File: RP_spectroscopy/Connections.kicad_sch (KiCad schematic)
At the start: 32 parts, among them J1 Extension connector 1, J2 Extension connector 2, J3 Conn_Coaxial, J4 Conn_Coaxial, J5 Conn_Coaxial, J6 Conn_Coaxial, J7 Conn_01x04_MountingPin, J8 Conn_01x04_MountingPin, U4 MC78L05_SOT89, U5 L79L05_SOT89

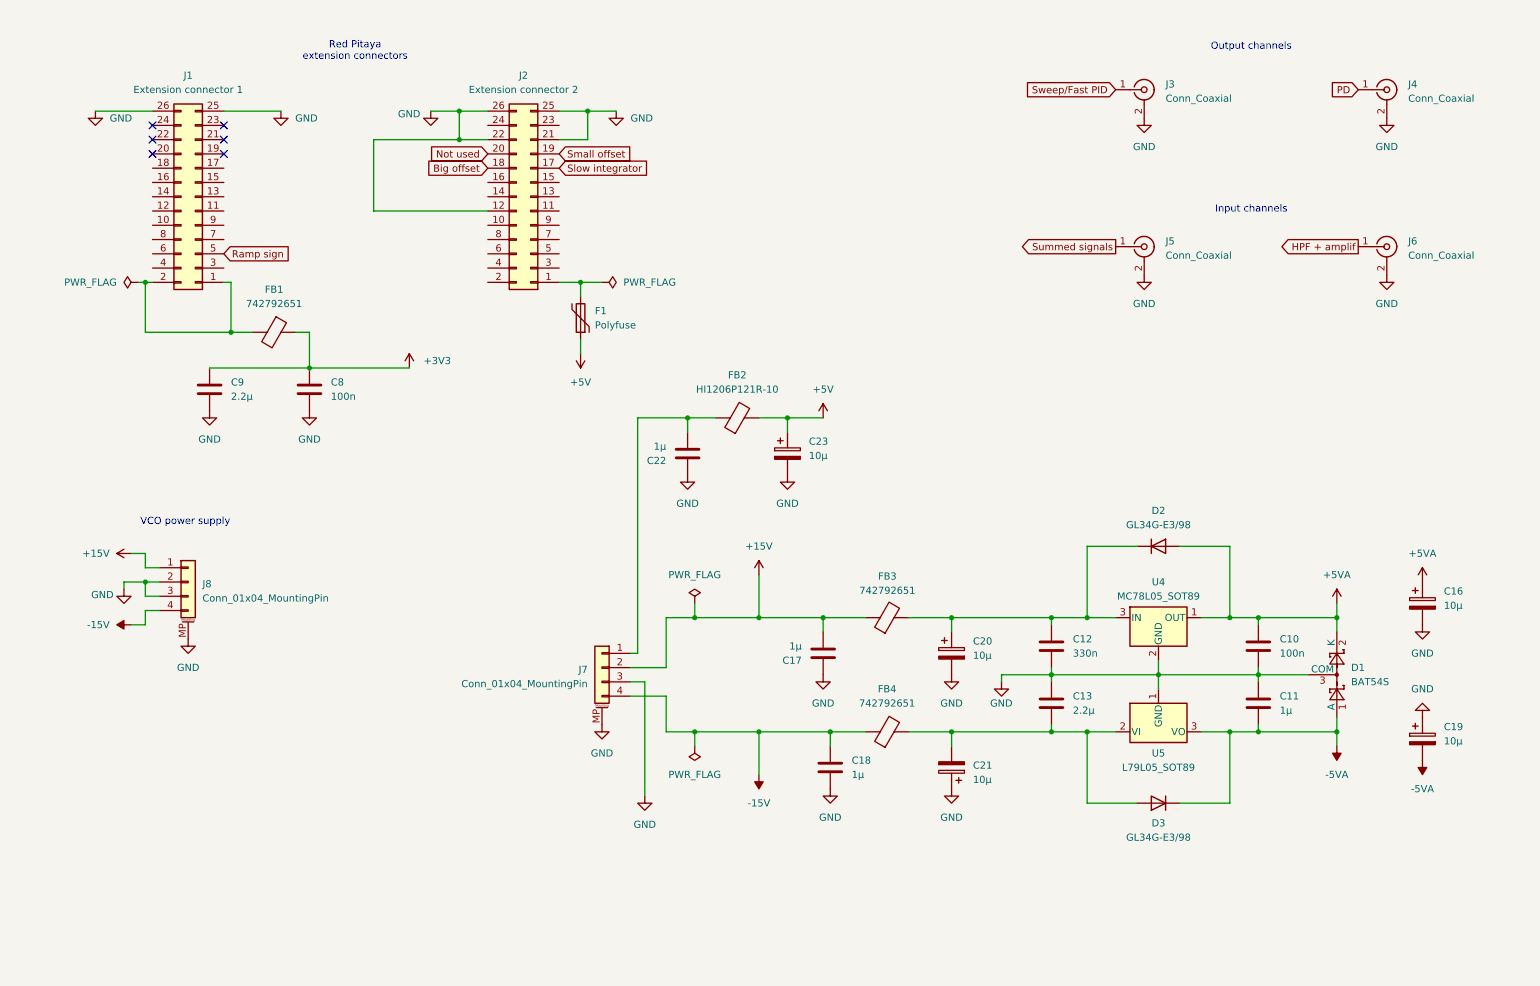
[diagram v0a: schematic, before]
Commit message: Check of the availability of all the components and of the footprints. Added the demultiplexer part of the circuit. Some graphical changes. Changed the values of some R in order to match the ones available in the officina elettronica.
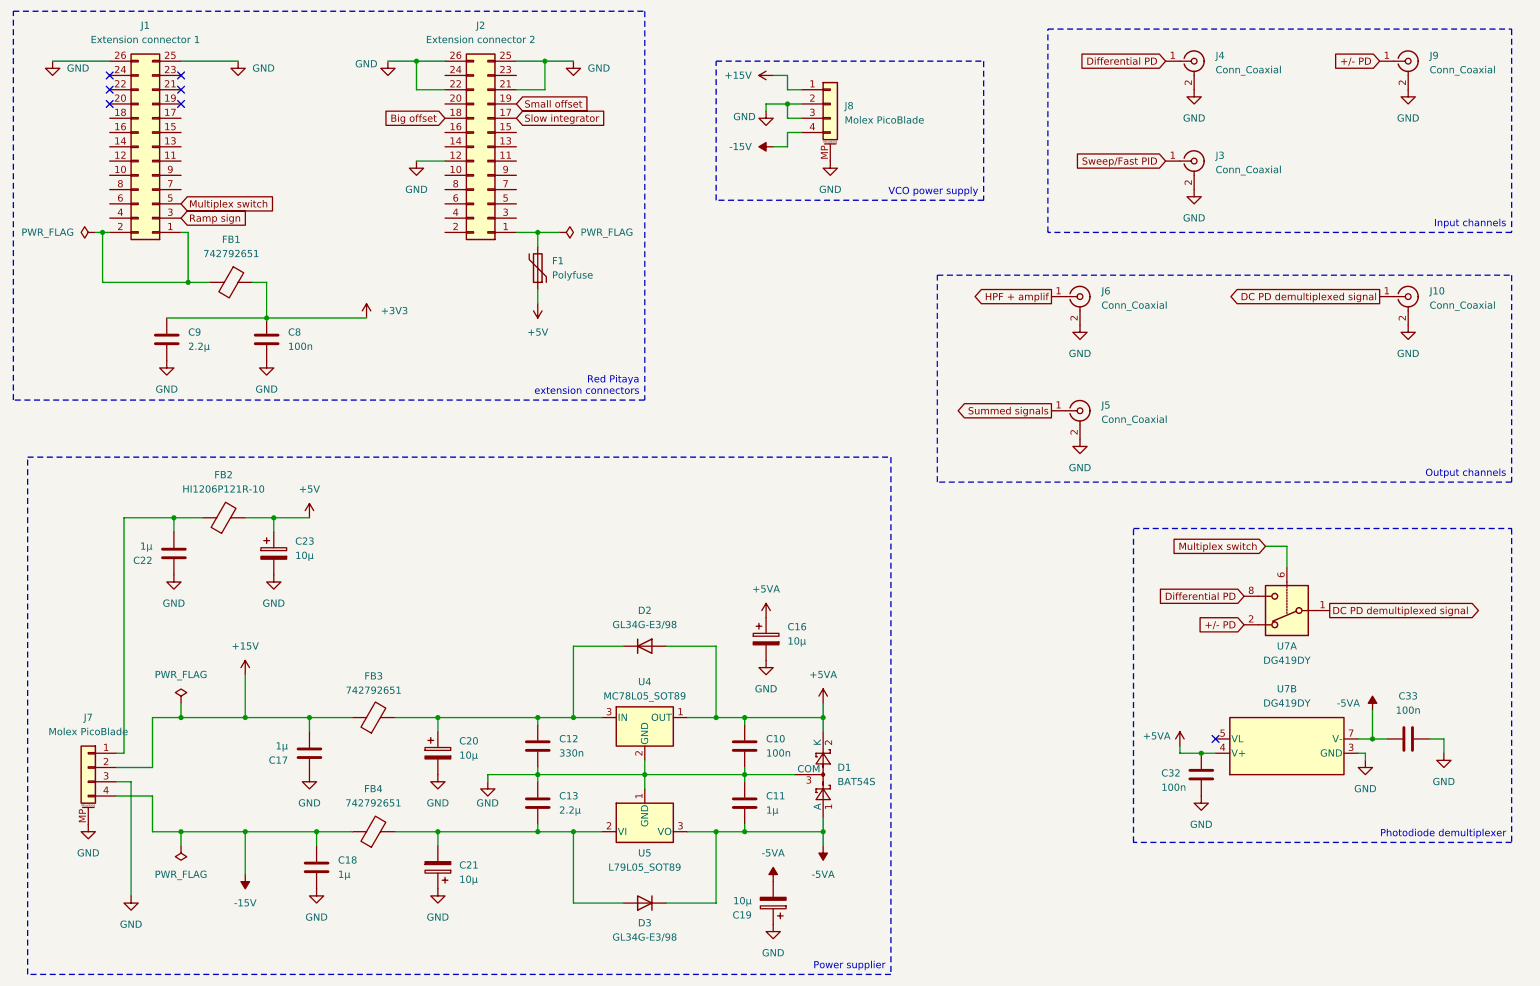
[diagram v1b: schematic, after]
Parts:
- added C32, C33: 100n, Capacitor_SMD:C_0805_2012Metric_Pad1.18x1.45mm_HandSolder, symbol Device:C
- added J10, J9: Conn_Coaxial, Connector_Coaxial:SMA_Molex_73251-1153_EdgeMount_Horizontal, symbol Connector:Conn_Coaxial
- added U7: DG419DY, Package_DIP:DIP-8_W7.62mm_Socket, symbol Analog_Switch:DG419xY
- C12: footprint Capacitor_SMD:C_0805_2012Metric_Pad1.18x1.45mm_HandSolder -> Capacitor_SMD:C_1206_3216Metric_Pad1.33x1.80mm_HandSolder
- C16, C19, C20, C21, C23: footprint Capacitor_SMD:CP_Elec_4x5.3 -> Capacitor_SMD:CP_Elec_6.3x5.7
- F1: footprint Fuse:Fuse_1812_4532Metric_Pad1.30x3.40mm_HandSolder -> Fuse:Fuse_0805_2012Metric_Pad1.15x1.40mm_HandSolder
- J7, J8: value Conn_01x04_MountingPin -> Molex PicoBlade
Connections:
- net +5VA: now also C32.1, U7.4 (V+)
- net -5VA: now also C33.1, U7.7 (V-)
- net GND: now also C32.2, C33.2, J10.2 (Ext), J9.2 (Ext), U7.3 (GND)
- net Ramp sign: now also J1.3 (Pin_3); no longer J1.5 (Pin_5)
- net Not used: no longer names the net of J2.20 (Pin_20)
- net PD renamed Differential PD
- net Differential PD: now also U7.8
- new net +/- PD: J9.1 (In), U7.2
- new net DC PD demultiplexed signal: J10.1 (In), U7.1
- new net Multiplex switch: J1.5 (Pin_5), U7.6
- no-connect marks 6 -> 7
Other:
- note removed: "Input channels"
- note removed: "Output channels"
- note removed: "Red Pitaya extension connectors"
- note removed: "VCO power supply"
- moved on the sheet: C10, C11, C12, C13, C16, C17, C18, C19, C20, C21, C22, C23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

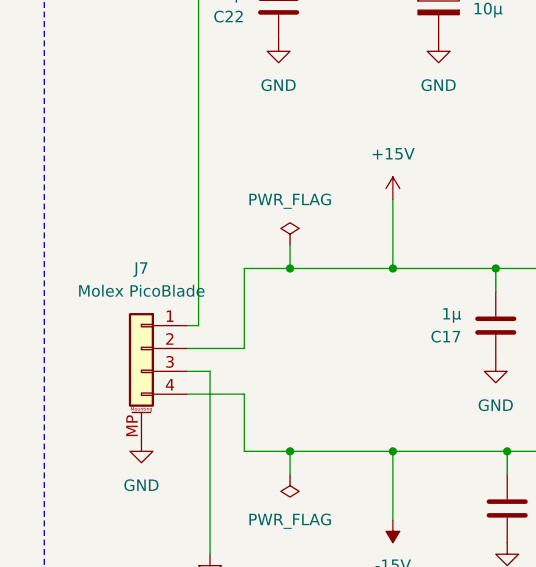
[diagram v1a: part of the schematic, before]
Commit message: Added the summator parameters. Started to do the wireings
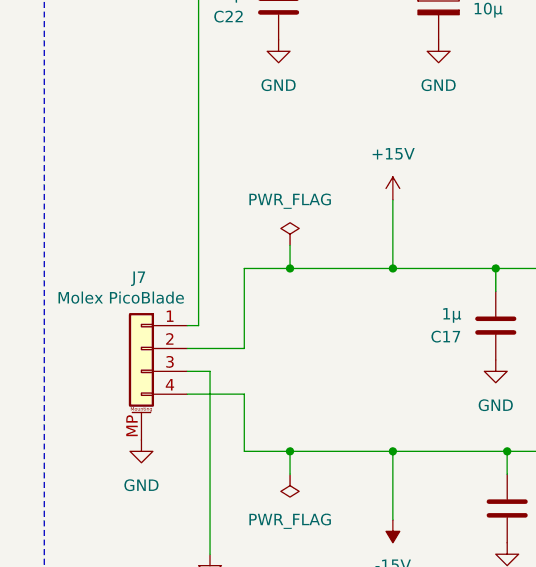
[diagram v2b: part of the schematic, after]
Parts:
- U7: footprint Package_DIP:DIP-8_W7.62mm_Socket -> Package_SO:SOIC-8_3.9x4.9mm_P1.27mm
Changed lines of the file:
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@@
 			)
 		)
-		(property "Footprint" "Package_DIP:DIP-8_W7.62mm_Socket"
+		(property "Footprint" "Package_SO:SOIC-8_3.9x4.9mm_P1.27mm"
 			(at 254.635 142.24 0)
 			(effects
@@
 			)
 		)
-		(property "Footprint" "Package_DIP:DIP-8_W7.62mm_Socket"
+		(property "Footprint" "Package_SO:SOIC-8_3.9x4.9mm_P1.27mm"
 			(at 237.49 107.315 0)
 			(effects
@@
 		(on_board yes)
 		(dnp no)
-		(fields_autoplaced yes)
 		(property "Reference" "J7"
-			(at 27.94 139.7 0)
+			(at 27.686 140.716 0)
 			(effects
 				(font
@@
 		)
 		(property "Value" "Molex PicoBlade"
-			(at 27.94 142.24 0)
-			(effects
-				(font
+			(at 25.654 143.002 0)
+			(effects
+				(font

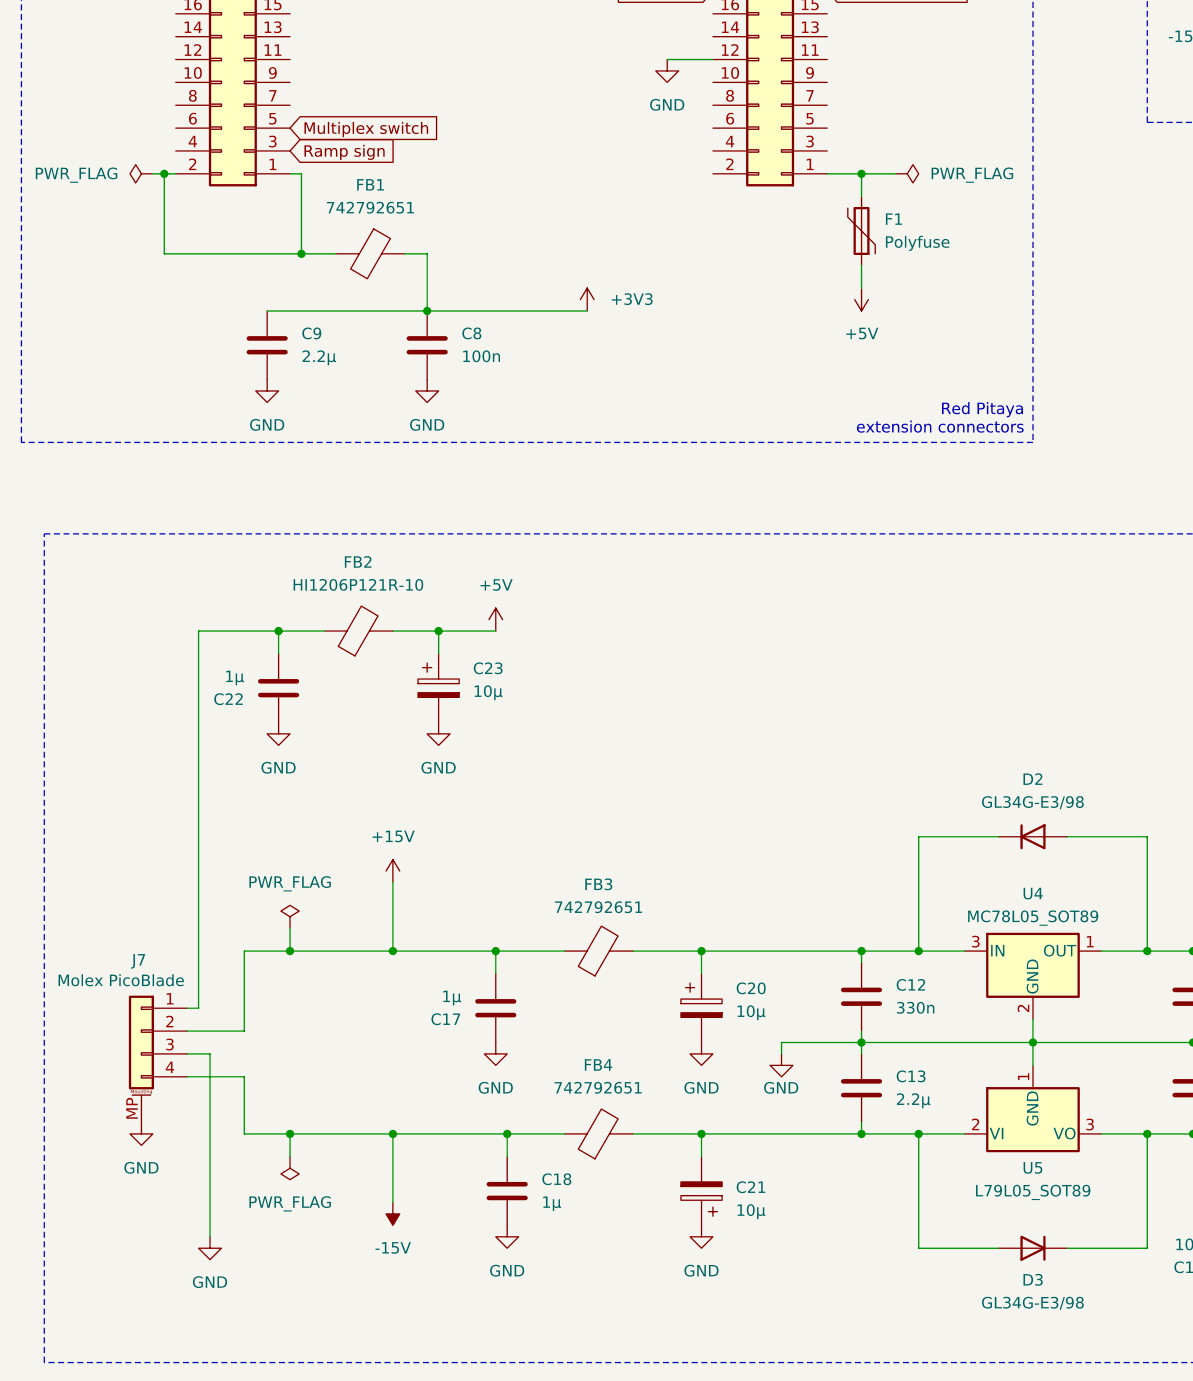
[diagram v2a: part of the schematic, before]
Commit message: Modified the input power connections in order to have the 5V to power the RP from the correct side
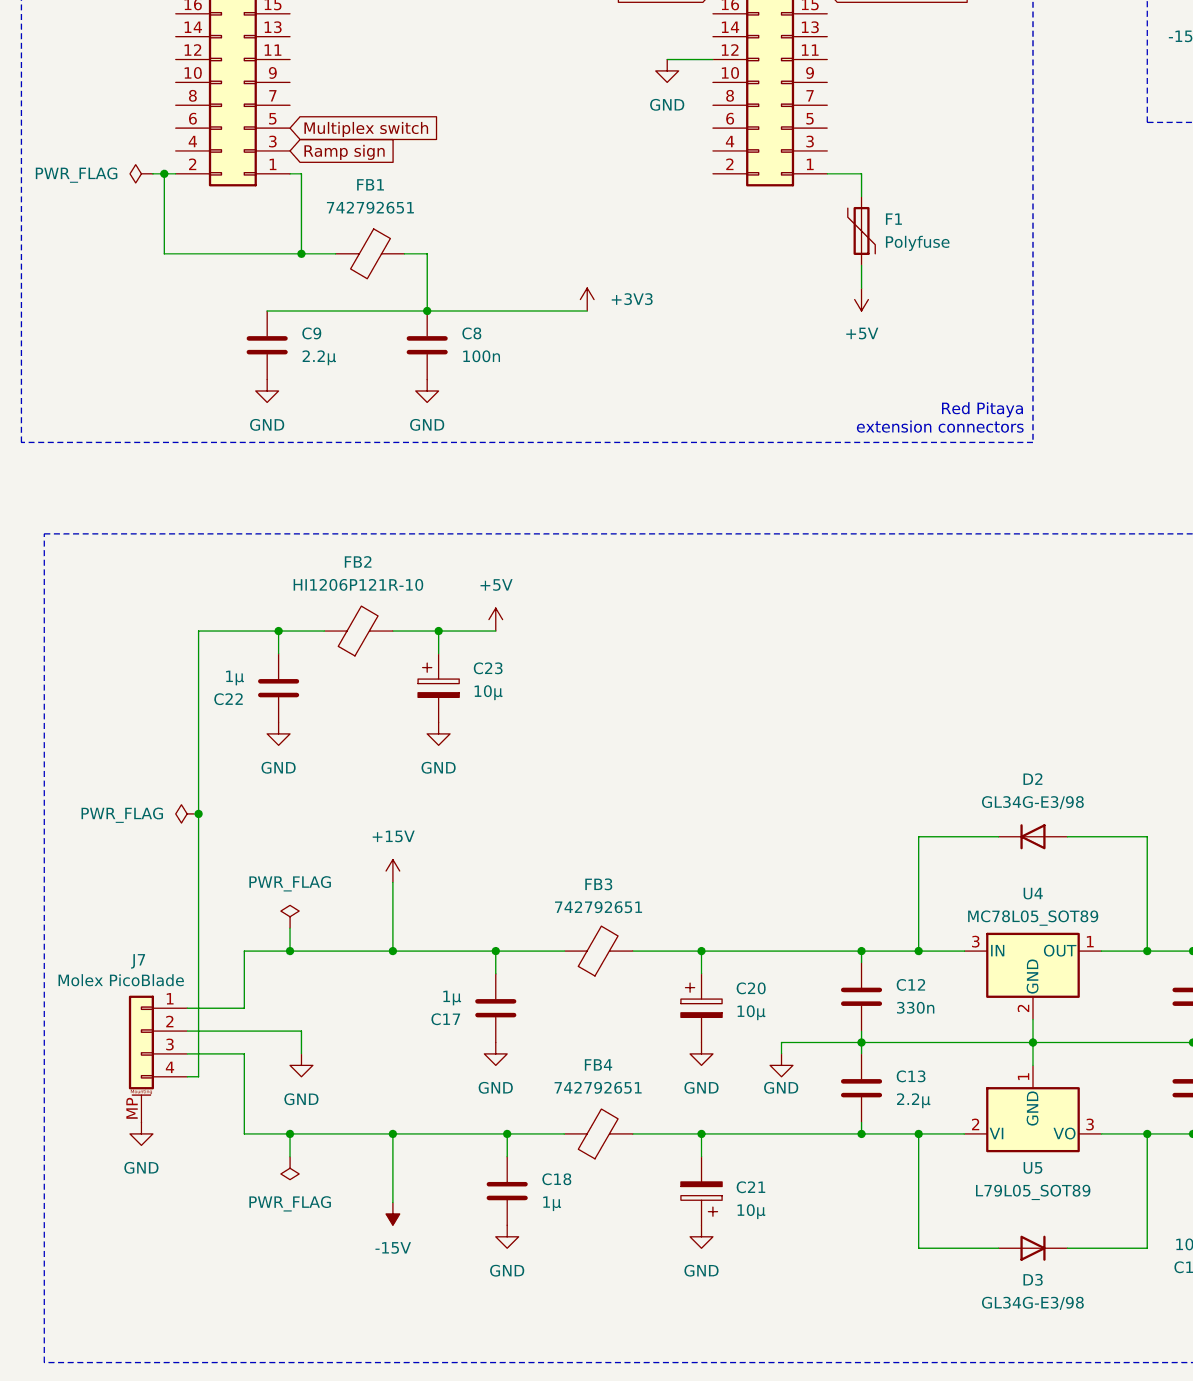
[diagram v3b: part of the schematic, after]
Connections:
- net +15V: now also J7.1 (Pin_1); no longer J7.2 (Pin_2)
- net -15V: now also J7.3 (Pin_3); no longer J7.4 (Pin_4)
- net GND: now also J7.2 (Pin_2); no longer J7.3 (Pin_3)
- net at C22.2, FB2.1: now also J7.4 (Pin_4); no longer J7.1 (Pin_1)
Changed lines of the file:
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@@
 	)
 	(junction
-		(at 107.95 53.34)
-		(diameter 0)
-		(color 0 0 0 0)
-	)
-	(junction
 		(at 44.45 139.7)
 		(diameter 0)
@@
 	)
 	(junction
+		(at 34.29 124.46)
+		(diameter 0)
+		(color 0 0 0 0)
+	)
+	(junction
 		(at 43.18 104.14)
 		(diameter 0)
@@
 	(wire
 		(pts
-			(xy 107.95 53.34) (xy 111.76 53.34)
-		)
-		(stroke
-			(width 0)
-			(type default)
-		)
-	)
-	(wire
-		(pts
 			(xy 123.19 127) (xy 114.3 127)
 		)
@@
 	(wire
 		(pts
-			(xy 35.56 151.13) (xy 35.56 171.45)
+			(xy 45.72 148.59) (xy 45.72 151.13)
 		)
 		(stroke
@@
 	(wire
 		(pts
-			(xy 39.37 153.67) (xy 39.37 160.02)
+			(xy 39.37 151.13) (xy 39.37 160.02)
 		)
 		(stroke
@@
 	(wire
 		(pts
-			(xy 39.37 139.7) (xy 39.37 148.59)
+			(xy 39.37 139.7) (xy 39.37 146.05)
 		)
 		(stroke
@@
 	(wire
 		(pts
-			(xy 33.02 151.13) (xy 35.56 151.13)
-		)
-		(stroke
-			(width 0)
-			(type default)
-		)
-	)
-	(wire
-		(pts
 			(xy 152.4 35.56) (xy 154.94 35.56)
 		)
@@
 	(wire
 		(pts
-			(xy 222.25 146.05) (xy 222.25 144.78)
+			(xy 33.02 146.05) (xy 39.37 146.05)
 		)
 		(stroke
@@
 	(wire
 		(pts
-			(xy 33.02 153.67) (xy 39.37 153.67)
+			(xy 222.25 146.05) (xy 222.25 144.78)
 		)
 		(stroke
@@
 	(wire
 		(pts
-			(xy 152.4 33.02) (xy 154.94 33.02)
+			(xy 34.29 124.46) (xy 34.29 153.67)
 		)
 		(stroke
@@
 	(wire
 		(pts
-			(xy 82.55 160.02) (xy 90.17 160.02)
+			(xy 152.4 33.02) (xy 154.94 33.02)
 		)
 		(stroke
@@
 	(wire
 		(pts
-			(xy 33.02 146.05) (xy 34.29 146.05)
+			(xy 82.55 160.02) (xy 90.17 160.02)
 		)
 		(stroke
@@
 	(wire
 		(pts
+			(xy 34.29 153.67) (xy 33.02 153.67)
+		)
+		(stroke
+			(width 0)
+			(type default)
+		)
+	)
+	(wire
+		(pts
 			(xy 114.3 160.02) (xy 119.38 160.02)
 		)
@@
 	(wire
 		(pts
-			(xy 39.37 148.59) (xy 33.02 148.59)
+			(xy 107.95 149.86) (xy 127 149.86)
 		)
 		(stroke
@@
 	(wire
 		(pts
-			(xy 107.95 149.86) (xy 127 149.86)
+			(xy 43.18 104.14) (xy 48.26 104.14)
 		)
 		(stroke
@@
 	(wire
 		(pts
-			(xy 43.18 104.14) (xy 48.26 104.14)
+			(xy 34.29 104.14) (xy 34.29 124.46)
 		)
 		(stroke
@@
 	(wire
 		(pts
-			(xy 34.29 146.05) (xy 34.29 104.14)
+			(xy 39.37 151.13) (xy 33.02 151.13)
 		)
 		(stroke
@@
 	(wire
 		(pts
+			(xy 45.72 148.59) (xy 33.02 148.59)
+		)
+		(stroke
+			(width 0)
+			(type default)
+		)
+	)
+	(wire
+		(pts
 			(xy 139.7 160.02) (xy 134.62 160.02)
 		)
@@
 	(symbol
 		(lib_id "power:PWR_FLAG")
-		(at 111.76 53.34 270)
+		(at 34.29 124.46 90)
 		(unit 1)
 		(exclude_from_sim no)
@@
 		(fields_autoplaced yes)
 		(property "Reference" "#FLG02"
-			(at 113.665 53.34 0)
+			(at 32.385 124.46 0)
 			(effects
 				(font
@@
 		)
 		(property "Value" "PWR_FLAG"
-			(at 115.57 53.3399 90)
+			(at 30.48 124.4599 90)
 			(effects
 				(font
@@
 		)
 		(property "Footprint" ""
-			(at 111.76 53.34 0)
+			(at 34.29 124.46 0)
 			(effects
 				(font
@@
 		)
 		(property "Datasheet" "~"
-			(at 111.76 53.34 0)
+			(at 34.29 124.46 0)
 			(effects
 				(font
@@
 		)
 		(property "Description" "Special symbol for telling ERC where power comes from"
-			(at 111.76 53.34 0)
+			(at 34.29 124.46 0)
 			(effects
 				(font
@@
 	(symbol
 		(lib_id "power:GND")
-		(at 35.56 171.45 0)
+		(at 45.72 151.13 0)
 		(unit 1)
 		(exclude_from_sim no)
@@
 		(fields_autoplaced yes)
 		(property "Reference" "#PWR058"
-			(at 35.56 177.8 0)
+			(at 45.72 157.48 0)
 			(effects
 				(font
@@
 		)
 		(property "Value" "GND"
-			(at 35.56 176.53 0)
+			(at 45.72 156.21 0)
 			(effects
 				(font
@@
 		)
 		(property "Footprint" ""
-			(at 35.56 171.45 0)
+			(at 45.72 151.13 0)
 			(effects
 				(font
@@
 		)
 		(property "Datasheet" ""
-			(at 35.56 171.45 0)
+			(at 45.72 151.13 0)
 			(effects
 				(font
@@
 		)
 		(property "Description" "Power symbol creates a global label with name \"GND\" , ground"
-			(at 35.56 171.45 0)
+			(at 45.72 151.13 0)
 			(effects
 				(font
